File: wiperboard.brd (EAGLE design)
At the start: 61.8 x 64.9 mm, 39 parts

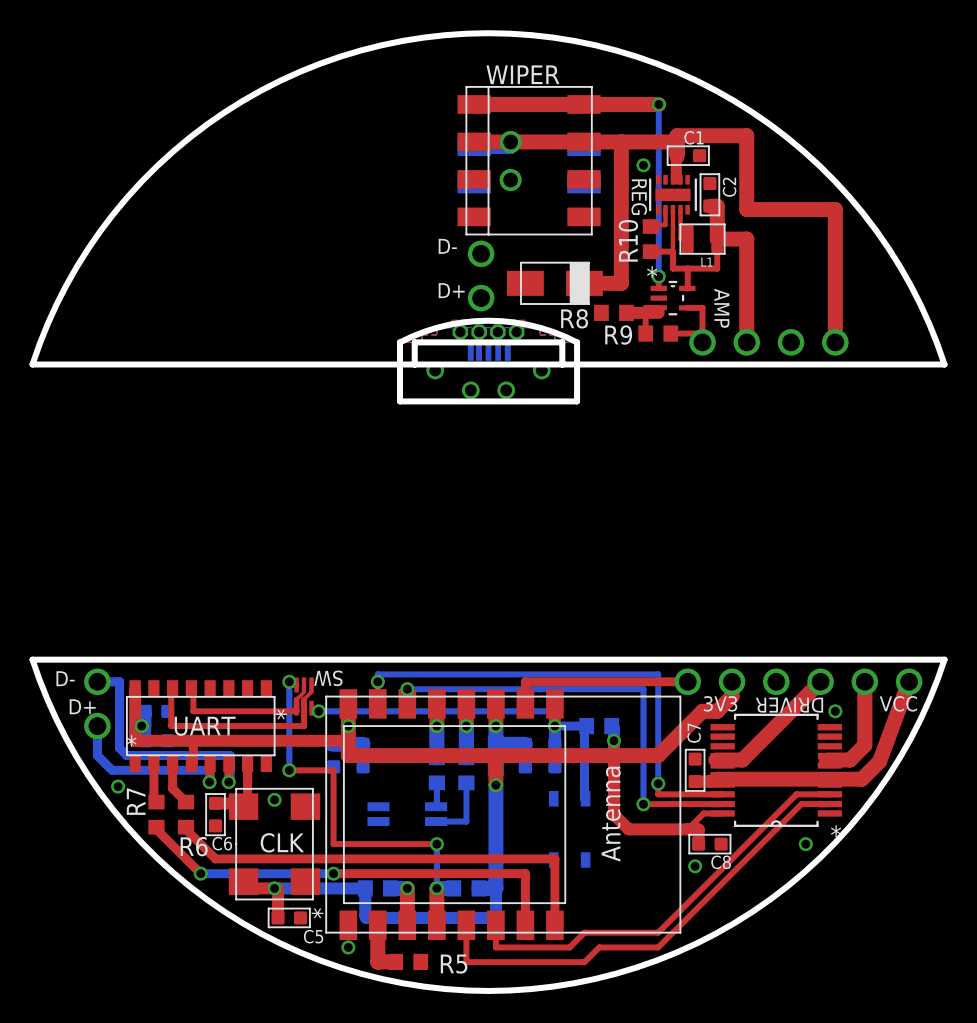
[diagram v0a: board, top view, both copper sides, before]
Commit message: split board into three parts, cam processed
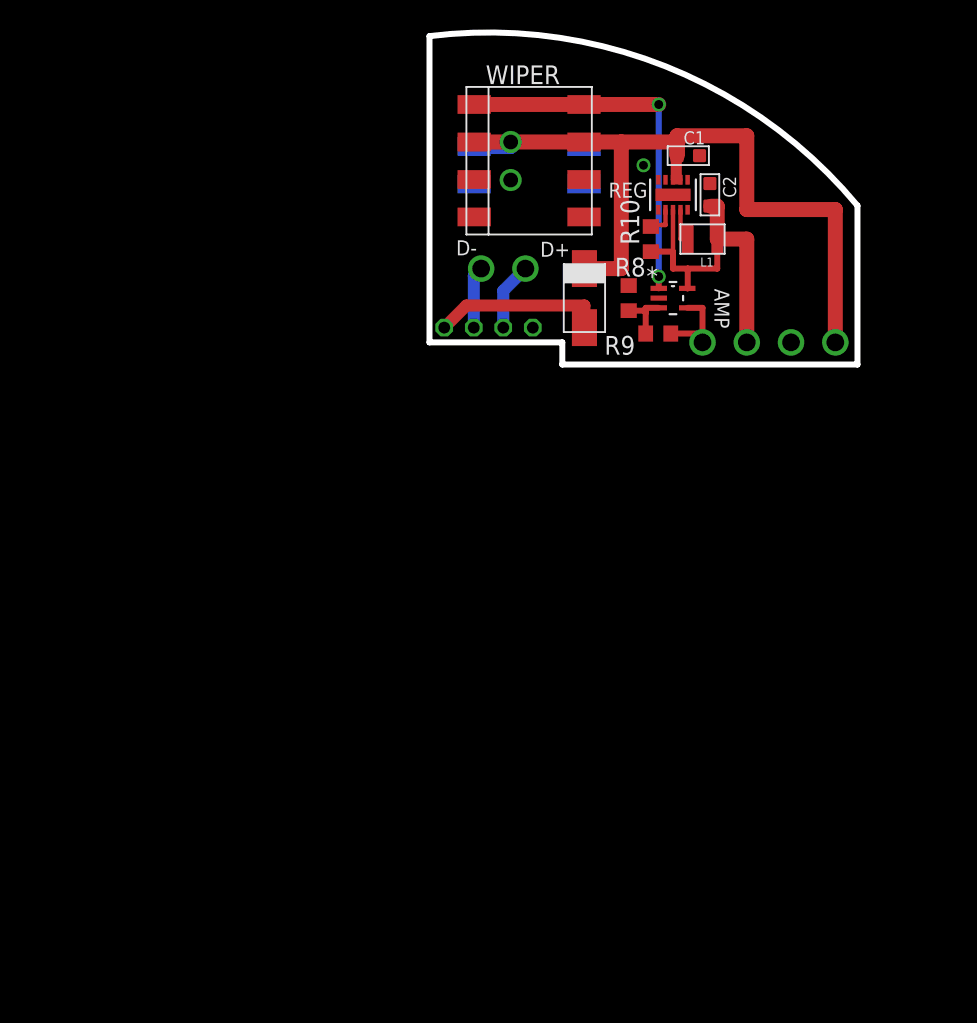
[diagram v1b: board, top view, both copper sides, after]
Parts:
- removed C10, C12, C4, C8, C9: 100nF, Seeed-OPL-Capacitor:C0603
- removed C11, C3, C7: 10uF, Seeed-OPL-Capacitor:C0603
- removed C5: 10pF, Seeed-OPL-Capacitor:C0603
- removed C6: 15pF, Seeed-OPL-Capacitor:C0603
- removed CLK: FXO_HC73, CUSTOM:4-SMD
- removed DRIVER: TB6593FNG, CUSTOM:SSOP-20
- removed ESP12: (no value), adafruit:ESP-12
- removed KEY: PTS810, CUSTOM:BUTTON
- removed MICRO-USB: ZX80-B-5P, CUSTOM:USB_VERT
- removed R1: 1k, resistor:R0603
- removed R11, R12: 100, resistor:R0603
- removed R2, R3, R4, R5: 10k, resistor:R0603
- removed R6, R7: 470, resistor:R0603
- removed SW: RN1906FE, CUSTOM:SOT-563
- removed U$2: BI_LED, CUSTOM:BI_LED
- removed UART: CH340G, CUSTOM:20-16
- moved D1 2.24 mm to (39.0, 47.0), turned to 270 degrees
- moved R8 1.41 mm to (42.0, 47.0), turned to 270 degrees
- moved U$3 0.30 mm to (32.5, 45.0)
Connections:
- removed net DTR: SW.1, SW.5, UART.13
- removed net EN: C12.2, ESP12.3, R1.2
- removed net GP0: ESP12.12, R3.2, SW.6
- removed net GP15: ESP12.10, R5.2
- removed net GP2: ESP12.11, R4.2
- removed net IN1: DRIVER.18, ESP12.7
- removed net IN2: DRIVER.19, ESP12.6
- removed net M1: DRIVER.6, DRIVER.7
- removed net M2: DRIVER.14, DRIVER.15
- removed net N$1: R7.2, UART.2
- removed net N$11: R11.1, U$2.2
- removed net N$12: R12.1, U$2.3
- removed net N$7: R6.2, UART.3
- removed net N$8: ESP12.5, R12.2
- removed net N$9: ESP12.4, R11.2
- removed net PWM: DRIVER.2, ESP12.13
- removed net RST: C9.2, ESP12.1, KEY.2, R2.2, SW.3
- removed net RTS: SW.2, SW.4, UART.14
- removed net RX: ESP12.15, R7.1
- removed net STBY: DRIVER.3, ESP12.14
- removed net TX: ESP12.16, R6.1
- removed net XI: C6.1, CLK.3, UART.7
- net +3V3: no longer C10.2, C11.2, C3.2, C4.2, C5.1, C8.2, CLK.4, DRIVER.20, ESP12.8, R1.1, R2.1, R3.1, R4.1, UART.16, UART.4
- net ADC: no longer ESP12.2
- net D+: no longer MICRO-USB.D+, UART.5
- net D-: no longer MICRO-USB.D-, UART.6
- net GND: no longer C10.1, C11.1, C12.1, C3.1, C4.1, C5.2, C6.2, C7.1, C8.1, C9.1, CLK.2, DRIVER.1, DRIVER.10, DRIVER.11, DRIVER.12, DRIVER.13, DRIVER.8, DRIVER.9, ESP12.9, KEY.4, MICRO-USB.GND, MICRO-USB.GND1, MICRO-USB.GND2, MICRO-USB.GND3, MICRO-USB.GND4, R5.1, U$2.1, U$2.4, UART.1
- net USB+: no longer MICRO-USB.VCC
- net VCC: no longer C7.2, DRIVER.16, DRIVER.17, DRIVER.4, DRIVER.5
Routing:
- net +3V3: track 134.0 -> 23.6 mm, vias 7 -> 1
- net IN1: track 33.5 -> 0.00 mm, vias 2 -> 0
- net PWM: track 31.6 -> 0.00 mm
- net TX: track 30.5 -> 0.00 mm
- net IN2: track 30.2 -> 0.00 mm, vias 2 -> 0
- net RX: track 29.9 -> 0.00 mm, vias 2 -> 0
- net STBY: track 28.4 -> 0.00 mm
- net GP0: track 28.4 -> 0.00 mm, vias 4 -> 0
- net RST: track 27.5 -> 0.00 mm, vias 2 -> 0
- net VCC: track 82.4 -> 57.0 mm, vias 3 -> 2
- net RTS: track 15.2 -> 0.00 mm
- net D-: track 16.8 -> 4.21 mm, vias 3 -> 1
- net ADC: track 18.0 -> 5.52 mm, vias 2 -> 1
- net USB+: track 0.00 -> 11.6 mm
- net DTR: track 11.2 -> 0.00 mm
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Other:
- board size 61.8 x 64.9 mm -> 29 x 22.5 mm
- board text removed: "3V3"
- board text removed: "VCC"

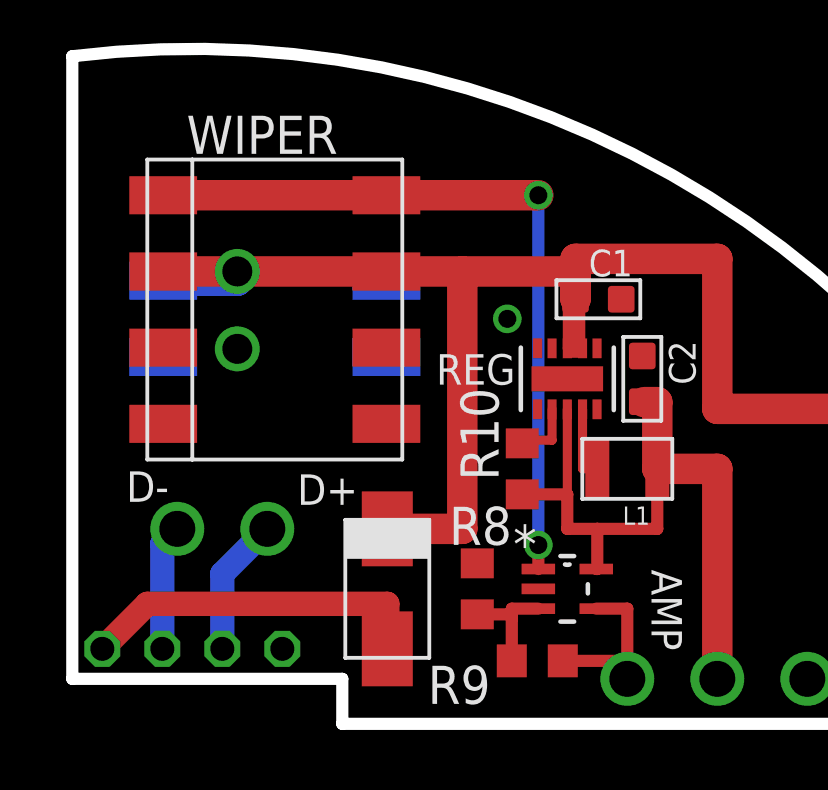
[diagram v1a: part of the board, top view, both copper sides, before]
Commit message: fixed intial board errors, including short, flipped usb, and missing trace
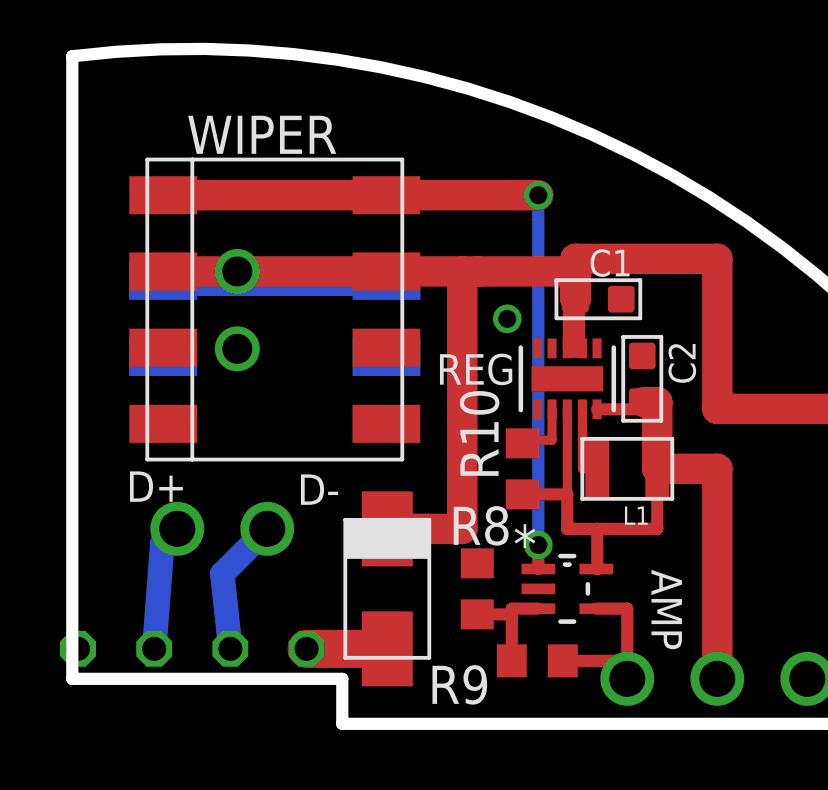
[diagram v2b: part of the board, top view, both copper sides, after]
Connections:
- net D+: now also U$3.2; no longer U$3.3
- net D-: now also U$3.3; no longer U$3.2
- net GND: now also CONN.P3, U$3.1, WIPER.P7, WIPER.P8; no longer U$3.4
- net N$5: now also WIPER.P5
- net USB+: now also U$3.4; no longer U$3.1
- net VCC: now also CONN.P4, WIPER.P6
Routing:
- net USB+: track 11.6 -> 2.69 mm
- net VCC: track 57.0 -> 65.0 mm
- net +3V3: track 23.6 -> 25.3 mm
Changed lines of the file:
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@@
 <setting verticaltext="up"/>
 </settings>
-<grid distance="1" unitdist="mm" unit="mm" style="lines" multiple="1" display="yes" altdistance="0.1" altunitdist="mm" altunit="mm"/>
+<grid distance="1" unitdist="mm" unit="mm" style="lines" multiple="1" display="no" altdistance="0.1" altunitdist="mm" altunit="mm"/>
 <layers>
 <layer number="1" name="Top" color="4" fill="1" visible="yes" active="yes"/>
@@
 <rectangle x1="44.9" y1="54.7" x2="45.6" y2="56.9" layer="1"/>
 <wire x1="28.5" y1="44" x2="37.5" y2="44" width="0.4064" layer="20"/>
-<text x="36" y="49.8" size="1.016" layer="21">D+</text>
-<text x="30.3" y="49.9" size="1.016" layer="21">D-</text>
+<text x="36" y="49.8" size="1.016" layer="21">D-</text>
+<text x="30.3" y="49.9" size="1.016" layer="21">D+</text>
 <wire x1="57.5" y1="53.266559375" x2="57.5" y2="42.5" width="0.4064" layer="20"/>
 <wire x1="28.5" y1="44" x2="28.5" y2="64.7529" width="0.4064" layer="20"/>
@@
 <contactref element="AMP" pad="2"/>
 <contactref element="WIPER" pad="P1"/>
-<contactref element="U$3" pad="4"/>
 <contactref element="WIPER" pad="P2"/>
 <contactref element="CONN" pad="P2"/>
@@
 <vertex x="57.5" y="53.266559375" curve="57.3546"/>
 </polygon>
+<contactref element="U$3" pad="1"/>
+<contactref element="WIPER" pad="P7"/>
+<contactref element="WIPER" pad="P8"/>
+<contactref element="CONN" pad="P3"/>
 </signal>
 <signal name="ADC">
@@
 <wire x1="45" y1="56.653" x2="45" y2="55.016" width="0.3048" layer="1"/>
 <wire x1="45" y1="55.016" x2="45.508" y2="55.016" width="0.3048" layer="1"/>
-<wire x1="34" y1="57.58" x2="41.5" y2="57.58" width="1.016" layer="1"/>
-<wire x1="41.5" y1="57.58" x2="45.274" y2="57.58" width="1.016" layer="1"/>
+<wire x1="34" y1="57.58" x2="38.97" y2="57.58" width="1.016" layer="1"/>
+<wire x1="38.97" y1="57.58" x2="41.5" y2="57.58" width="1.016" layer="1"/>
+<wire x1="41.5" y1="57.58" x2="42" y2="57.58" width="1.016" layer="1"/>
+<wire x1="42" y1="57.58" x2="45.274" y2="57.58" width="1.016" layer="1"/>
 <wire x1="45.274" y1="57.58" x2="45.274" y2="56.653" width="1.016" layer="1"/>
 <wire x1="39" y1="49" x2="41.5" y2="49" width="1.016" layer="1"/>
@@
 <wire x1="45.274" y1="58" x2="45.274" y2="56.653" width="1.016" layer="1"/>
 <wire x1="31.53" y1="57.27" x2="34" y2="57.27" width="1.016" layer="16"/>
-<wire x1="34" y1="57.27" x2="34" y2="57.58" width="1.016" layer="16"/>
 <via x="34" y="57.58" extent="1-16" drill="1"/>
 <wire x1="34" y1="57.58" x2="31.53" y2="57.58" width="1.016" layer="1"/>
+<contactref element="WIPER" pad="P6"/>
+<wire x1="38.97" y1="57.58" x2="42" y2="57.58" width="0.4064" layer="1"/>
+<contactref element="CONN" pad="P4"/>
+<wire x1="38.97" y1="57.27" x2="34" y2="57.27" width="1.016" layer="16"/>
+<wire x1="34" y1="57.27" x2="34" y2="57.58" width="1.016" layer="16"/>
 </signal>
 <signal name="+3V3">
@@
 <wire x1="45.9652" y1="47.6604" x2="46" y2="47.6604" width="0.4064" layer="1"/>
 <wire x1="46" y1="47.6604" x2="46" y2="49" width="0.4064" layer="1"/>
-<wire x1="45" y1="52.984" x2="45.9906" y2="52.984" width="0" layer="19" extent="1-1"/>
+<wire x1="45.9906" y1="52.984" x2="47.5" y2="52.984" width="0.4064" layer="1"/>
+<wire x1="47.5" y1="52.984" x2="47.5" y2="53.238" width="0.4064" layer="1"/>
 </signal>
 <signal name="N$2">
@@
 <wire x1="45.508" y1="51" x2="46" y2="51" width="0.3048" layer="1"/>
 </signal>
-<signal name="D+">
+<signal name="D-">
 <contactref element="U$3" pad="3"/>
 <via x="35" y="49" extent="1-16" drill="1.2"/>
-<wire x1="33.5" y1="45" x2="33.5" y2="47.5" width="0.8128" layer="16"/>
+<wire x1="33.77" y1="45" x2="33.5" y2="47.5" width="0.8128" layer="16"/>
 <wire x1="33.5" y1="47.5" x2="35" y2="49" width="0.8128" layer="16"/>
 </signal>
-<signal name="D-">
+<signal name="D+">
 <contactref element="U$3" pad="2"/>
 <via x="32" y="49" extent="1-16" drill="1.2"/>
-<wire x1="31.5" y1="45" x2="31.5" y2="48.5" width="0.8128" layer="16"/>
+<wire x1="31.23" y1="45" x2="31.5" y2="48.5" width="0.8128" layer="16"/>
 <wire x1="31.5" y1="48.5" x2="32" y2="49" width="0.8128" layer="16"/>
 </signal>
@@
 <contactref element="AMP" pad="1"/>
 <contactref element="WIPER" pad="P4"/>
-<wire x1="31.53" y1="60.12" x2="44.0348" y2="60.12" width="1.016" layer="1"/>
+<wire x1="31.53" y1="60.12" x2="38.97" y2="60.12" width="1.016" layer="1"/>
+<wire x1="38.97" y1="60.12" x2="44.0348" y2="60.12" width="1.016" layer="1"/>
 <wire x1="44.0348" y1="60.12" x2="44.0348" y2="48.4604" width="0.4064" layer="16"/>
 <via x="44.0348" y="60.12" extent="1-16" drill="0.6"/>
 <via x="44.0348" y="48.4604" extent="1-16" drill="0.6"/>
 <wire x1="44.0348" y1="48.4604" x2="44.0348" y2="47.6604" width="0.4064" layer="1"/>
+<contactref element="WIPER" pad="P5"/>
 </signal>
 <signal name="N$6">
@@
 <signal name="USB+">
 <contactref element="D1" pad="AN"/>
-<contactref element="U$3" pad="1"/>
-<wire x1="29.5" y1="45" x2="31" y2="46.5" width="0.8128" layer="1"/>
-<wire x1="31" y1="46.5" x2="39" y2="46.5" width="0.8128" layer="1"/>
-<wire x1="39" y1="46.5" x2="39" y2="45" width="0.8128" layer="1"/>
+<contactref element="U$3" pad="4"/>
+<wire x1="36.31" y1="45" x2="39" y2="45" width="1.27" layer="1"/>
 </signal>
 </signals>

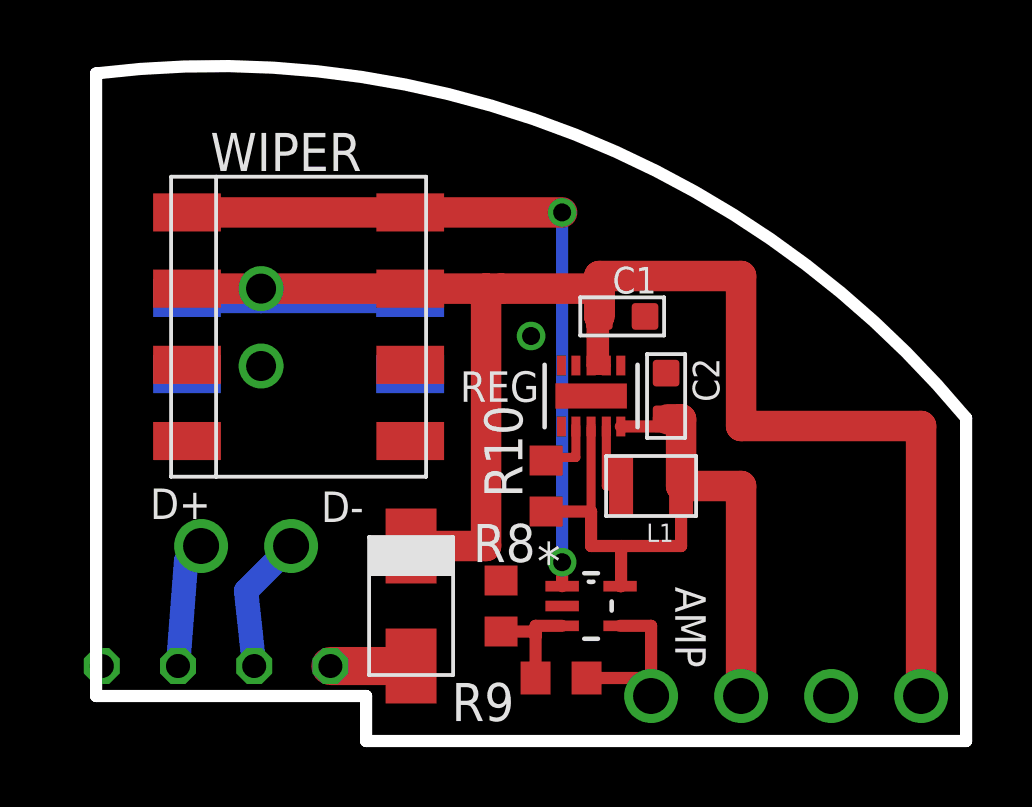
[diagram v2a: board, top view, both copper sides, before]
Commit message: fixed collision issue
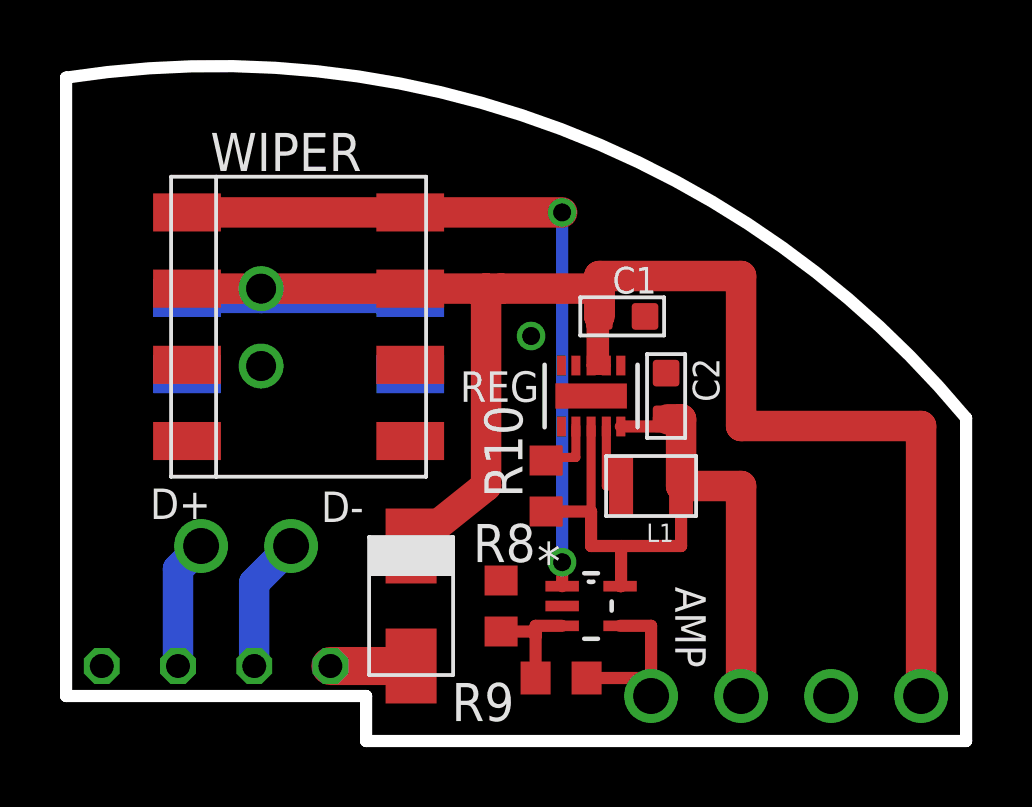
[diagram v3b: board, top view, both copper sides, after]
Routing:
- net VCC: track 65.0 -> 60.7 mm
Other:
- board size 29 x 22.5 mm -> 30 x 22.5 mm
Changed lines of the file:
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@@
 <rectangle x1="52.751" y1="49.6934" x2="54.2242" y2="49.7442" layer="200"/>
 <wire x1="37.5" y1="42.5" x2="57.5" y2="42.5" width="0.4064" layer="20"/>
-<wire x1="28.5" y1="64.7529" x2="57.5" y2="53.266559375" width="0.4064" layer="20" curve="-57.3546"/>
+<wire x1="27.5" y1="64.61308125" x2="57.5" y2="53.266559375" width="0.4064" layer="20" curve="-59.134746"/>
 <rectangle x1="44.9" y1="54.7" x2="45.6" y2="56.9" layer="1"/>
-<wire x1="28.5" y1="44" x2="37.5" y2="44" width="0.4064" layer="20"/>
+<wire x1="27.5" y1="44" x2="37.5" y2="44" width="0.4064" layer="20"/>
 <text x="36" y="49.8" size="1.016" layer="21">D-</text>
 <text x="30.3" y="49.9" size="1.016" layer="21">D+</text>
 <wire x1="57.5" y1="53.266559375" x2="57.5" y2="42.5" width="0.4064" layer="20"/>
-<wire x1="28.5" y1="44" x2="28.5" y2="64.7529" width="0.4064" layer="20"/>
+<wire x1="27.5" y1="44" x2="27.5" y2="64.61308125" width="0.4064" layer="20"/>
 <wire x1="37.5" y1="44" x2="37.5" y2="42.5" width="0.4064" layer="20"/>
 </plain>
@@
 <via x="34" y="55" extent="1-16" drill="1"/>
 <polygon width="0.254" layer="16" thermals="no">
-<vertex x="28.5" y="64.7529"/>
-<vertex x="28.5" y="44"/>
+<vertex x="27.5" y="64.61308125"/>
+<vertex x="27.5" y="44"/>
 <vertex x="37.5" y="44"/>
 <vertex x="37.5" y="42.5"/>
 <vertex x="57.5" y="42.5"/>
-<vertex x="57.5" y="53.266559375" curve="57.3546"/>
+<vertex x="57.5" y="53.266559375" curve="59.134746"/>
 </polygon>
 <polygon width="0.254" layer="1" thermals="no">
-<vertex x="28.5" y="64.7529"/>
-<vertex x="28.5" y="44"/>
+<vertex x="27.5" y="64.61308125"/>
+<vertex x="27.5" y="44"/>
 <vertex x="37.5" y="44"/>
 <vertex x="37.5" y="42.5"/>
 <vertex x="57.5" y="42.5"/>
-<vertex x="57.5" y="53.266559375" curve="57.3546"/>
+<vertex x="57.5" y="53.266559375" curve="59.134746"/>
 </polygon>
 <contactref element="U$3" pad="1"/>
@@
 <wire x1="42" y1="57.58" x2="45.274" y2="57.58" width="1.016" layer="1"/>
 <wire x1="45.274" y1="57.58" x2="45.274" y2="56.653" width="1.016" layer="1"/>
-<wire x1="39" y1="49" x2="41.5" y2="49" width="1.016" layer="1"/>
-<wire x1="41.5" y1="49" x2="41.5" y2="57.58" width="1.016" layer="1"/>
+<wire x1="39" y1="49" x2="41.5" y2="51" width="1.016" layer="1"/>
+<wire x1="41.5" y1="51" x2="41.5" y2="57.58" width="1.016" layer="1"/>
 <wire x1="56" y1="44" x2="56" y2="53" width="1.016" layer="1"/>
 <wire x1="56" y1="53" x2="50" y2="53" width="1.016" layer="1"/>
@@
 <wire x1="34" y1="57.58" x2="31.53" y2="57.58" width="1.016" layer="1"/>
 <contactref element="WIPER" pad="P6"/>
-<wire x1="38.97" y1="57.58" x2="42" y2="57.58" width="0.4064" layer="1"/>
 <contactref element="CONN" pad="P4"/>
 <wire x1="38.97" y1="57.27" x2="34" y2="57.27" width="1.016" layer="16"/>
@@
 <contactref element="U$3" pad="3"/>
 <via x="35" y="49" extent="1-16" drill="1.2"/>
-<wire x1="33.77" y1="45" x2="33.5" y2="47.5" width="0.8128" layer="16"/>
-<wire x1="33.5" y1="47.5" x2="35" y2="49" width="0.8128" layer="16"/>
+<wire x1="33.77" y1="45" x2="33.77" y2="47.77" width="1.016" layer="16"/>
+<wire x1="33.77" y1="47.77" x2="35" y2="49" width="1.016" layer="16"/>
 </signal>
 <signal name="D+">
 <contactref element="U$3" pad="2"/>
 <via x="32" y="49" extent="1-16" drill="1.2"/>
-<wire x1="31.23" y1="45" x2="31.5" y2="48.5" width="0.8128" layer="16"/>
-<wire x1="31.5" y1="48.5" x2="32" y2="49" width="0.8128" layer="16"/>
+<wire x1="31.23" y1="45" x2="31.23" y2="48.23" width="1.016" layer="16"/>
+<wire x1="31.23" y1="48.23" x2="32" y2="49" width="1.016" layer="16"/>
 </signal>
 <signal name="N$5">
